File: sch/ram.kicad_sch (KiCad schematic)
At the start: 26 parts

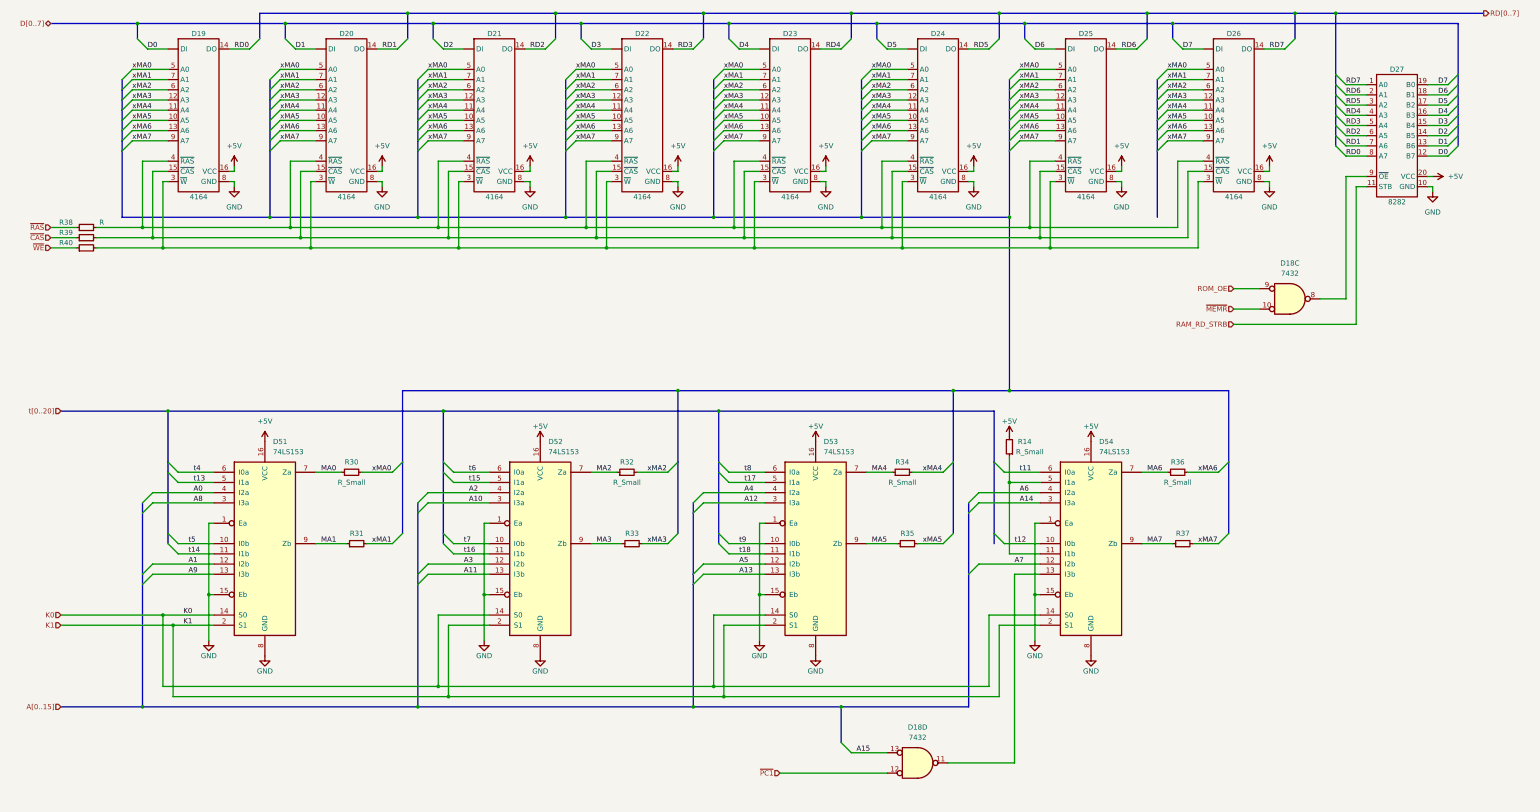
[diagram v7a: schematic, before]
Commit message: Schematics complete
Todo:
- part values
- full review
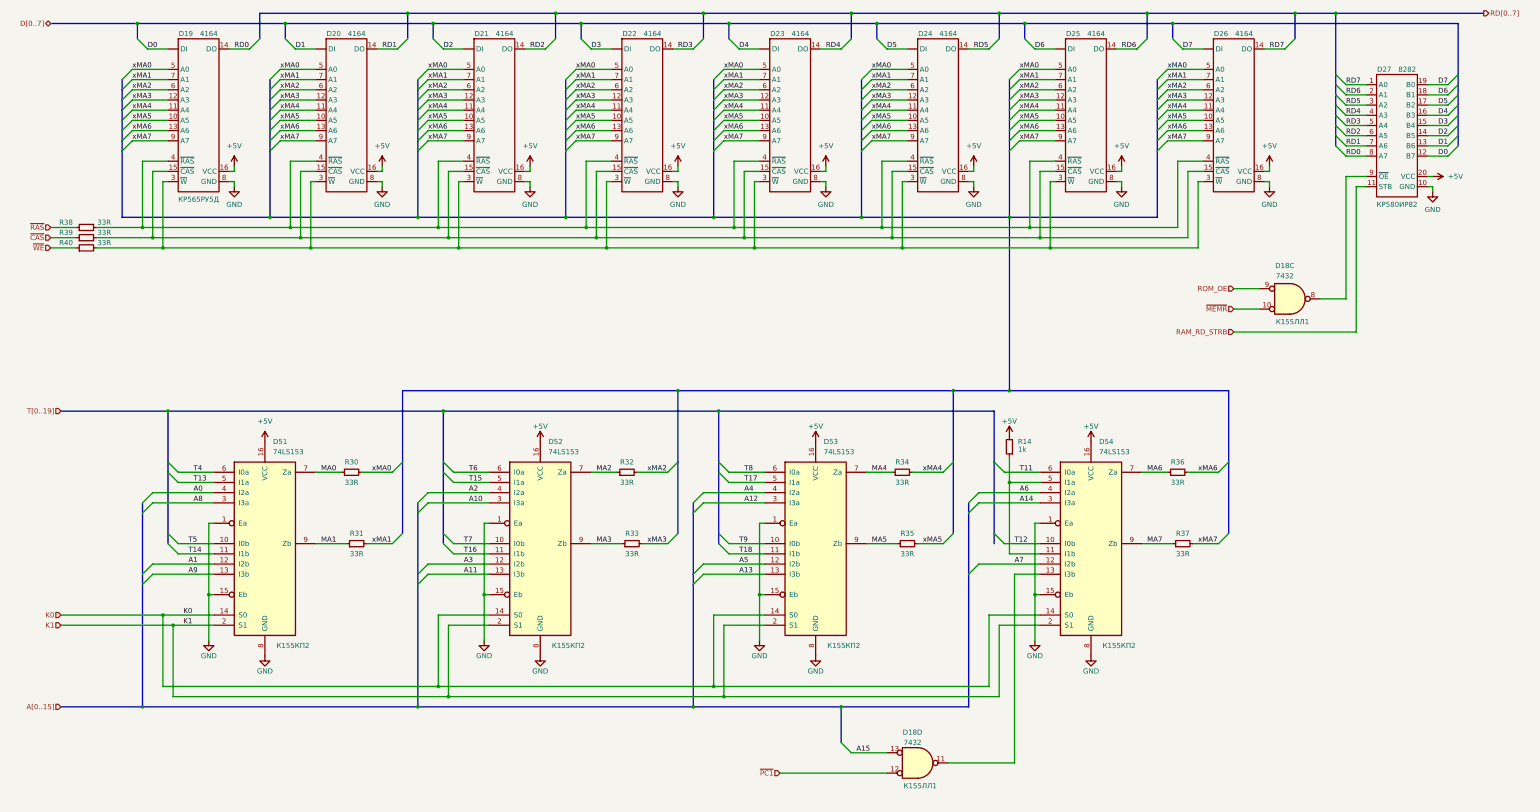
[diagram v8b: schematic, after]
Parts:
- D18: CCCP (none) -> К155ЛЛ1
- D19: CCCP (none) -> КР565РУ5Д
- D27: CCCP (none) -> КР580ИР82
- D51, D52, D53, D54: CCCP (none) -> К155КП2
- R14: value R_Small -> 1k
- R30, R32, R34, R36: value R_Small -> 33R
- R31, R33, R35, R37, R39, R40: value ~ -> 33R
- R38: value R -> 33R
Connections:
- net t11 renamed T11
- net t12 renamed T12
- net t13 renamed T13
- net t14 renamed T14
- net t15 renamed T15
- net t16 renamed T16
- net t17 renamed T17
- net t18 renamed T18
- net t4 renamed T4
- net t5 renamed T5
- net t6 renamed T6
- net t7 renamed T7
- net t8 renamed T8
- net t9 renamed T9
